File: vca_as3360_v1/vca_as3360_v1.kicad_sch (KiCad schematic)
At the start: 12 parts, among them J1 Conn_02x05_Odd_Even

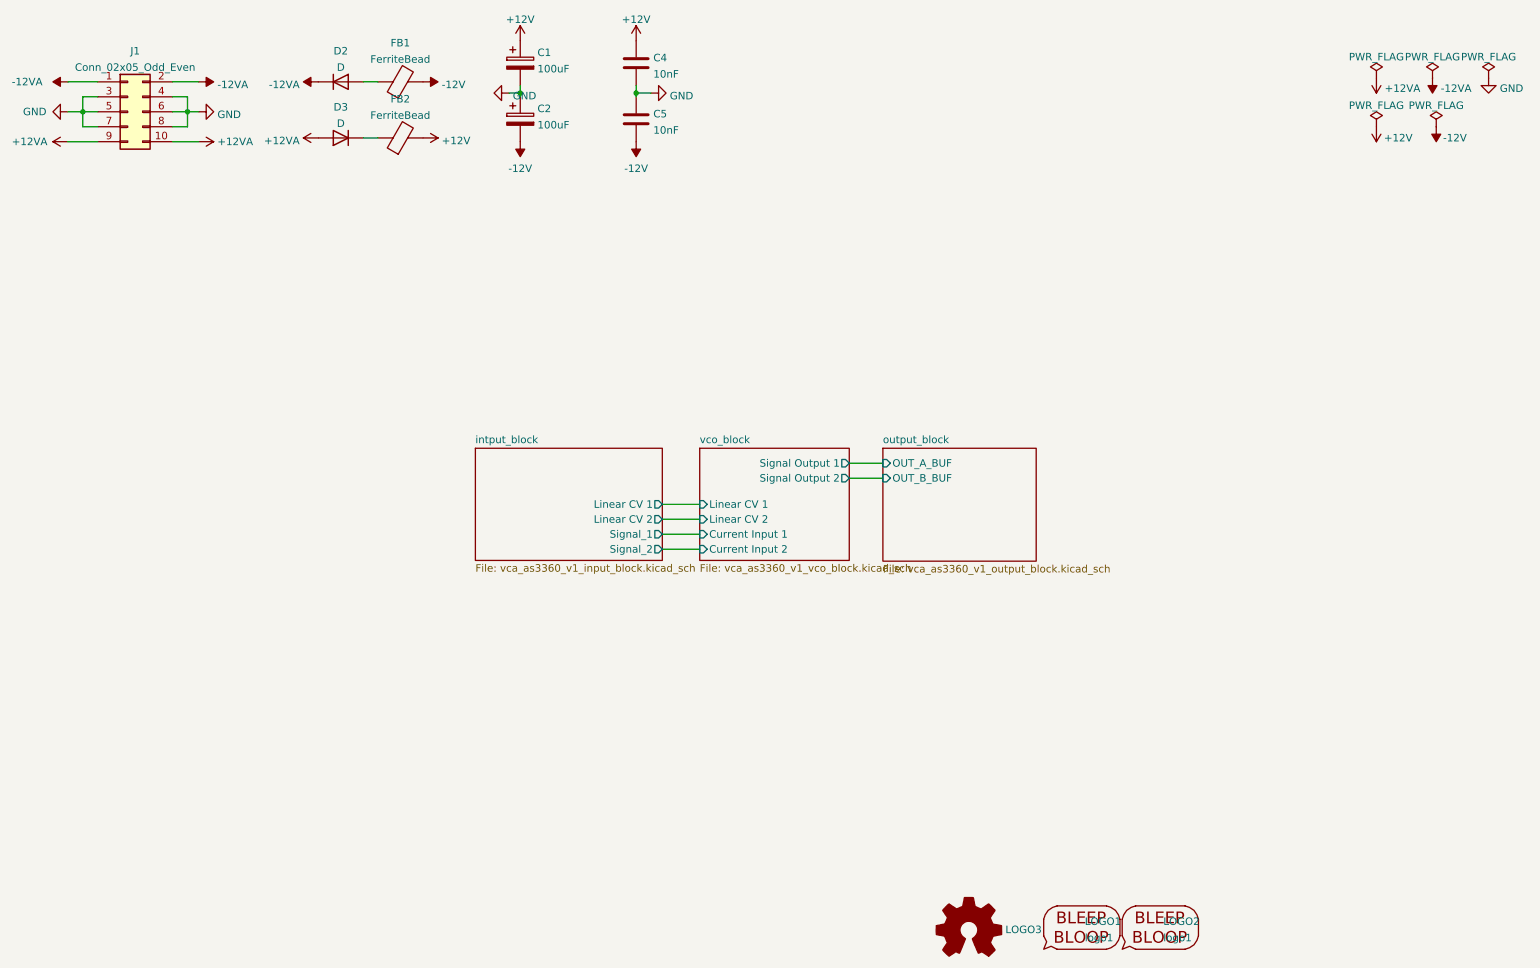
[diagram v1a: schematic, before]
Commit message: Geographic rename and silkscreen cleanup
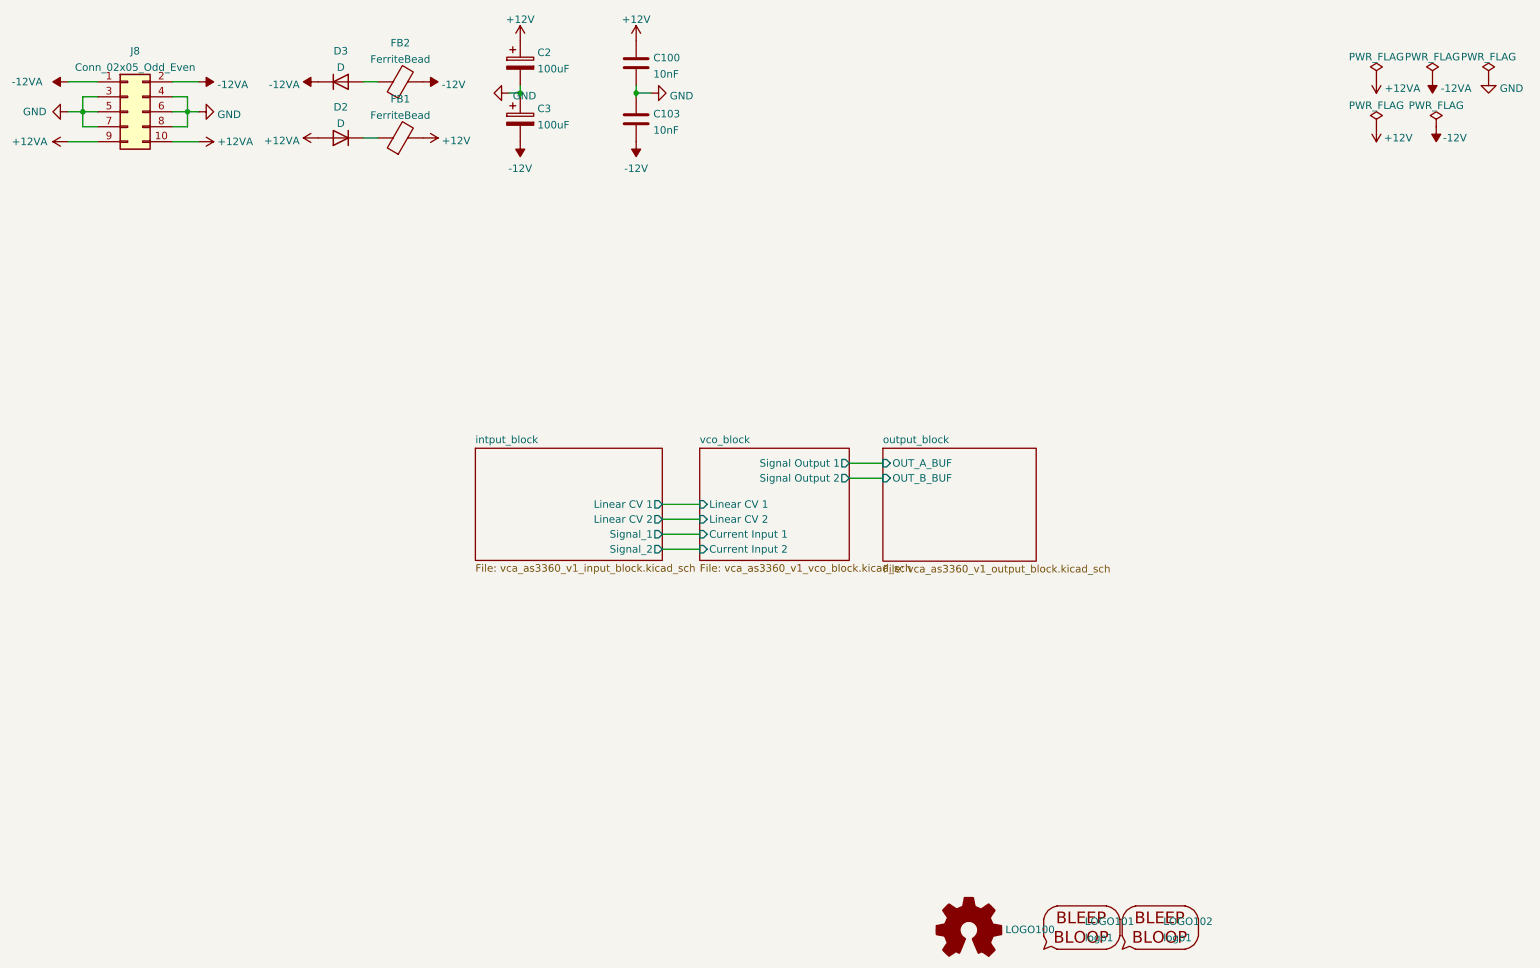
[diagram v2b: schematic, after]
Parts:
- renumbered C4 to C100, C5 to C103, C1 to C2, C2 to C3, D3 to D2, D2 to D3, FB2 to FB1, FB1 to FB2, J1 to J8, LOGO3 to LOGO100, LOGO1 to LOGO101, LOGO2 to LOGO102

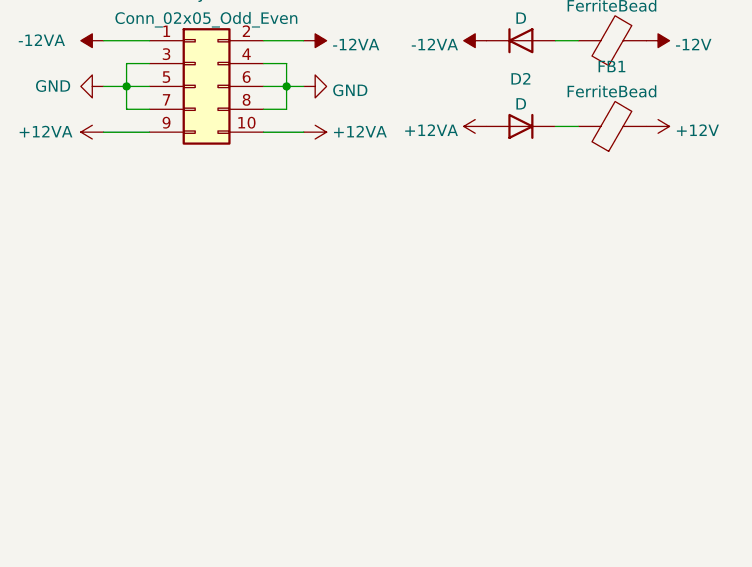
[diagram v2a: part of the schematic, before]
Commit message: Add jumper points for passing power to another pcb
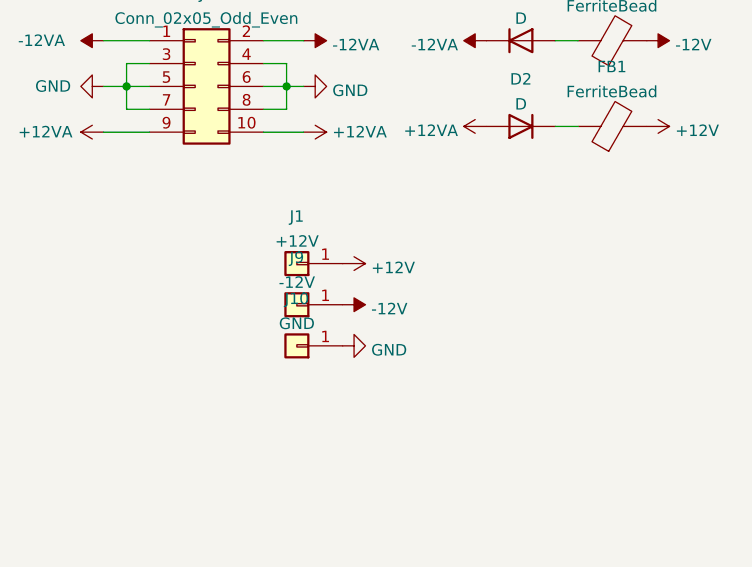
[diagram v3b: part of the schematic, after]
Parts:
- added J1: +12V, Connector_PinHeader_2.54mm:PinHeader_1x01_P2.54mm_Vertical, symbol Connector_Generic:Conn_01x01
- added J10: GND, Connector_PinHeader_2.54mm:PinHeader_1x01_P2.54mm_Vertical, symbol Connector_Generic:Conn_01x01
- added J9: -12V, Connector_PinHeader_2.54mm:PinHeader_1x01_P2.54mm_Vertical, symbol Connector_Generic:Conn_01x01
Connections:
- net +12V: now also J1.1 (Pin_1)
- net -12V: now also J9.1 (Pin_1)
- net GND: now also J10.1 (Pin_1)
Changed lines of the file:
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@@
     (pin "2")
+  )
+  (symbol (lib_id "Connector_Generic:Conn_01x01") (at 52.578 59.182 180) (unit 1)
+    (in_bom yes) (on_board yes) (fields_autoplaced)
+    (property "Reference" "J9" (id 0) (at 52.578 53.9455 0))
+    (property "Value" "-12V" (id 1) (at 52.578 56.7206 0))
+    (property "Footprint" "Connector_PinHeader_2.54mm:PinHeader_1x01_P2.54mm_Vertical" (id 2) (at 52.578 59.182 0)
+      (effects (font (size 1.27 1.27)) hide)
+    )
+    (property "Datasheet" "~" (id 3) (at 52.578 59.182 0)
+      (effects (font (size 1.27 1.27)) hide)
+    )
+    (pin "1")
   )
   (symbol (lib_id "My Stuff:Logo_Open_Hardware_Small") (at 184.15 173.99 0) (unit 1)
@@
     (pin "2")
   )
+  (symbol (lib_id "power:GND") (at 57.658 63.754 90) (unit 1)
+    (in_bom yes) (on_board yes) (fields_autoplaced)
+    (property "Reference" "#PWR08" (id 0) (at 64.008 63.754 0)
+      (effects (font (size 1.27 1.27)) hide)
+    )
+    (property "Value" "GND" (id 1) (at 60.833 64.233 90)
+      (effects (font (size 1.27 1.27)) (justify right))
+    )
+    (property "Footprint" "" (id 2) (at 57.658 63.754 0)
+      (effects (font (size 1.27 1.27)) hide)
+    )
+    (property "Datasheet" "" (id 3) (at 57.658 63.754 0)
+      (effects (font (size 1.27 1.27)) hide)
+    )
+    (pin "1")
+  )
+  (symbol (lib_id "Connector_Generic:Conn_01x01") (at 52.578 54.61 180) (unit 1)
+    (in_bom yes) (on_board yes) (fields_autoplaced)
+    (property "Reference" "J1" (id 0) (at 52.578 49.3735 0))
+    (property "Value" "+12V" (id 1) (at 52.578 52.1486 0))
+    (property "Footprint" "Connector_PinHeader_2.54mm:PinHeader_1x01_P2.54mm_Vertical" (id 2) (at 52.578 54.61 0)
+      (effects (font (size 1.27 1.27)) hide)
+    )
+    (property "Datasheet" "~" (id 3) (at 52.578 54.61 0)
+      (effects (font (size 1.27 1.27)) hide)
+    )
+    (pin "1")
+  )
   (symbol (lib_id "power:+12V") (at 253.365 37.465 180) (unit 1)
     (in_bom yes) (on_board yes)
@@
     (pin "1")
   )
+  (symbol (lib_id "power:+12V") (at 57.658 54.61 270) (unit 1)
+    (in_bom yes) (on_board yes) (fields_autoplaced)
+    (property "Reference" "#PWR06" (id 0) (at 53.848 54.61 0)
+      (effects (font (size 1.27 1.27)) hide)
+    )
+    (property "Value" "+12V" (id 1) (at 60.833 55.089 90)
+      (effects (font (size 1.27 1.27)) (justify left))
+    )
+    (property "Footprint" "" (id 2) (at 57.658 54.61 0)
+      (effects (font (size 1.27 1.27)) hide)
+    )
+    (property "Datasheet" "" (id 3) (at 57.658 54.61 0)
+      (effects (font (size 1.27 1.27)) hide)
+    )
+    (pin "1")
+  )
   (symbol (lib_id "power:PWR_FLAG") (at 253.365 29.21 0) (unit 1)
     (in_bom yes) (on_board yes) (fields_autoplaced)
@@
     )
     (property "Datasheet" "" (id 3) (at 53.34 29.845 0)
+      (effects (font (size 1.27 1.27)) hide)
+    )
+    (pin "1")
+  )
+  (symbol (lib_id "power:-12V") (at 57.658 59.182 270) (unit 1)
+    (in_bom yes) (on_board yes) (fields_autoplaced)
+    (property "Reference" "#PWR07" (id 0) (at 60.198 59.182 0)
+      (effects (font (size 1.27 1.27)) hide)
+    )
+    (property "Value" "-12V" (id 1) (at 60.833 59.661 90)
+      (effects (font (size 1.27 1.27)) (justify left))
+    )
+    (property "Footprint" "" (id 2) (at 57.658 59.182 0)
+      (effects (font (size 1.27 1.27)) hide)
+    )
+    (property "Datasheet" "" (id 3) (at 57.658 59.182 0)
+      (effects (font (size 1.27 1.27)) hide)
+    )
+    (pin "1")
+  )
+  (symbol (lib_id "Connector_Generic:Conn_01x01") (at 52.578 63.754 180) (unit 1)
+    (in_bom yes) (on_board yes) (fields_autoplaced)
+    (property "Reference" "J10" (id 0) (at 52.578 58.5175 0))
+    (property "Value" "GND" (id 1) (at 52.578 61.2926 0))
+    (property "Footprint" "Connector_PinHeader_2.54mm:PinHeader_1x01_P2.54mm_Vertical" (id 2) (at 52.578 63.754 0)
+      (effects (font (size 1.27 1.27)) hide)
+    )
+    (property "Datasheet" "~" (id 3) (at 52.578 63.754 0)
       (effects (font (size 1.27 1.27)) hide)
     )
@@
       (reference "#PWR05") (unit 1) (value "-12V") (footprint "")
     )
+    (path "/72732eef-3039-4172-aefb-c082832523a1"
+      (reference "#PWR06") (unit 1) (value "+12V") (footprint "")
+    )
+    (path "/e4175fa6-5caf-4643-b89b-134d2ab0b3da"
+      (reference "#PWR07") (unit 1) (value "-12V") (footprint "")
+    )
+    (path "/3cda2794-a109-443a-89ca-fa2a5745b7d6"
+      (reference "#PWR08") (unit 1) (value "GND") (footprint "")
+    )
     (path "/e7e02353-c97f-4d53-a805-83749d0c218d/2c804411-5881-4034-ae50-e08fbf39cc68"
       (reference "#PWR0101") (unit 1) (value "-12V") (footprint "")
@@
       (reference "FB2") (unit 1) (value "FerriteBead") (footprint "Inductor_THT:L_Axial_L6.6mm_D2.7mm_P2.54mm_Vertical_Vishay_IM-2")
     )
+    (path "/4cdfab87-b4c2-412a-82a8-a62a2f37a29f"
+      (reference "J1") (unit 1) (value "+12V") (footprint "Connector_PinHeader_2.54mm:PinHeader_1x01_P2.54mm_Vertical")
+    )
     (path "/35ee76ea-1c3d-4f41-b24f-ac923be7cf97/50eca47b-9ab2-4dcf-aed1-34cbb4d2fa77"
       (reference "J2") (unit 1) (value "OUT_1") (footprint "My Stuff:Jack_3.5mm_MJ-355W_Vertical")
@@
       (reference "J8") (unit 1) (value "Conn_02x05_Odd_Even") (footprint "Connector_IDC:IDC-Header_2x05_P2.54mm_Vertical")
     )
+    (path "/2391b830-8b67-4aaa-bbae-94fa5617d94a"
+      (reference "J9") (unit 1) (value "-12V") (footprint "Connector_PinHeader_2.54mm:PinHeader_1x01_P2.54mm_Vertical")
+    )
+    (path "/e433aa36-7312-4a61-90eb-3fcc05a3bddd"
+      (reference "J10") (unit 1) (value "GND") (footprint "Connector_PinHeader_2.54mm:PinHeader_1x01_P2.54mm_Vertical")
+    )
     (path "/25af93ef-5019-41b0-99ec-301965180b81"
